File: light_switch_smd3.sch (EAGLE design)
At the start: 33 parts, among them U1 ESP8266_ESP-01

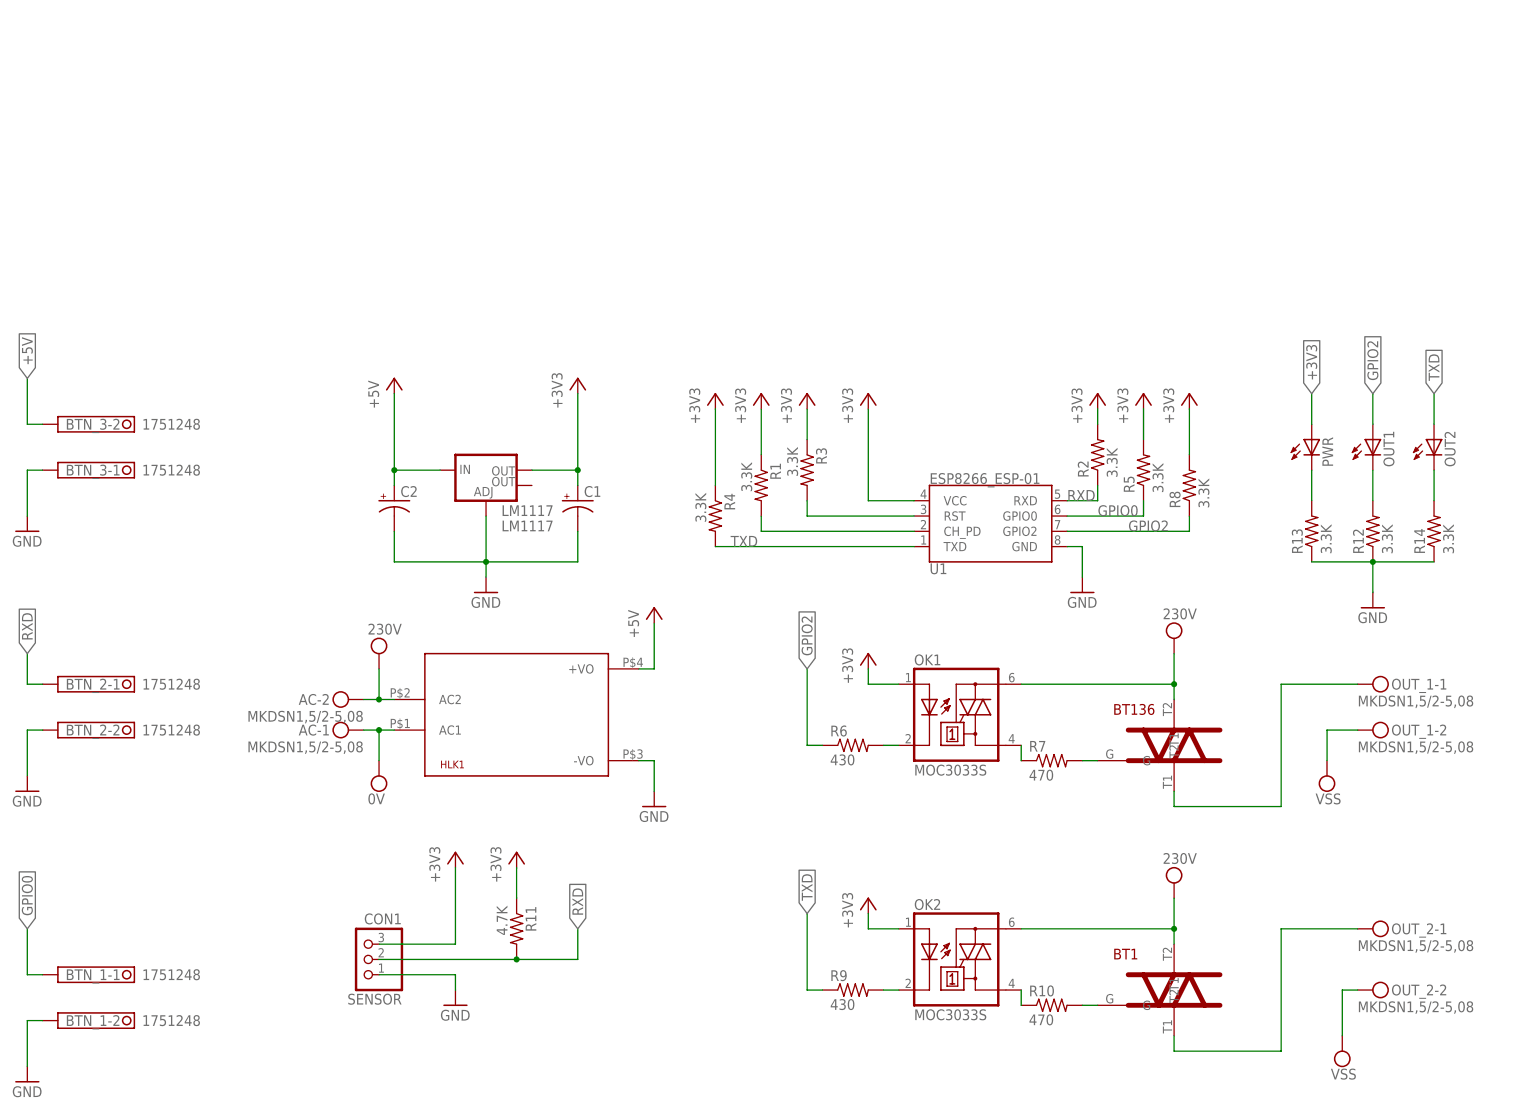
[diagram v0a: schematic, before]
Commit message: added pcf8574 due to undefined state of GPIOs during boot
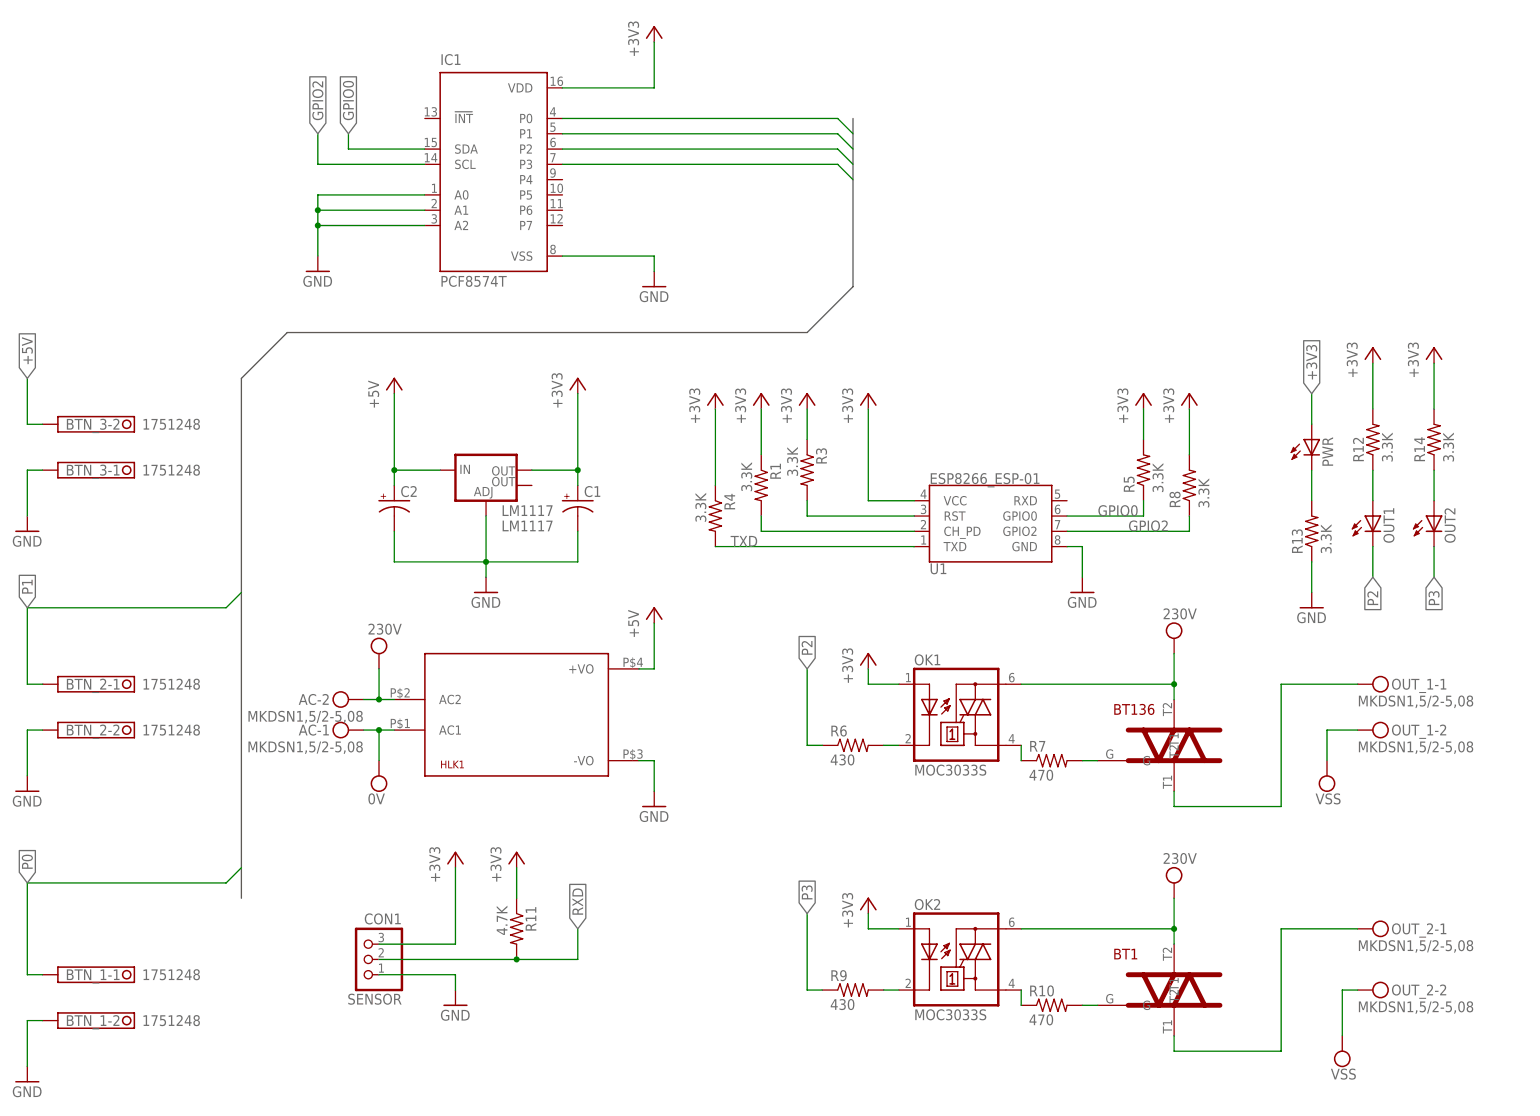
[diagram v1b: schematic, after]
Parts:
- removed R2: 3.3K, resistor:R-US_R1206
- added IC1: PCF8574T, micro-philips:PCF8574T
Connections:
- new net P0: BTN_1-1.K, IC1.P0
- new net P1: BTN_2-1.K, IC1.P1
- new net P2: IC1.P2, OUT1.C, R6.1
- new net P3: IC1.P3, OUT2.C, R9.1
- net +3V3: now also IC1.VDD, R12.2, R14.2; no longer R2.2
- net GND: now also IC1.A0, IC1.A1, IC1.A2, IC1.VSS; no longer R12.1, R14.1
- net GPIO0: now also IC1.SDA; no longer BTN_1-1.K
- net GPIO2: now also IC1.SCL; no longer OUT1.A, R6.1
- net N$11: now also OUT2.A, R14.1; no longer OUT2.C, R14.2
- net N$9: now also OUT1.A, R12.1; no longer OUT1.C, R12.2
- net RXD: no longer BTN_2-1.K, R2.1, U1.RXD
- net TXD: no longer OUT2.A, R9.1
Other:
- moved on the sheet: OUT1, OUT2, R12, R14

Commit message: DRC checked, no airwires
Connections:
- net RXD: now also U1.RXD
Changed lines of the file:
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@@
 <label x="101.6" y="35.56" size="1.778" layer="95" rot="R90" xref="yes"/>
+</segment>
+<segment>
+<pinref part="U1" gate="G$1" pin="RXD"/>
+<wire x1="182.88" y1="106.68" x2="185.42" y2="106.68" width="0.1524" layer="91"/>
+<wire x1="185.42" y1="106.68" x2="185.42" y2="116.84" width="0.1524" layer="91"/>
+<label x="185.42" y="116.84" size="1.778" layer="95" rot="R90" xref="yes"/>
 </segment>
 </net>

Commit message: added pinheader and small fixes
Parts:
- removed BTN_1, BTN_2: 1751248, con-phoenix-350:1751248
- added F1: (no value), fuse:TE5
- added JP1: (no value), pinhead:PINHD-1X4
- added X1: 1751251, con-phoenix-350:1751251
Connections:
- new net P4: IC1.P4, JP1.1
- new net P5: IC1.P5, JP1.2
- new net P6: IC1.P6, JP1.3
- new net P7: IC1.P7, JP1.4
- new net V230FUSE: BT1.T2, BT136.T2, F1.1, HLK1.AC2, OK1.A2, OK2.A2
- net GND: now also X1-2.K; no longer BTN_1-2.K, BTN_2-2.K
- net N$4: now also OUT_1-2.KL; no longer OUT_1-1.KL
- net N$8: now also OUT_2-2.KL; no longer OUT_2-1.KL
- net P0: now also X1-3.K; no longer BTN_1-1.K
- net P1: now also X1-1.K; no longer BTN_2-1.K
- net VPP: now also F1.2; no longer BT1.T2, BT136.T2, HLK1.AC2, OK1.A2, OK2.A2
- net VSS: now also OUT_1-1.KL, OUT_2-1.KL; no longer OUT_1-2.KL, OUT_2-2.KL
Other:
- moved on the sheet: OUT_1-1, OUT_1-2, OUT_2-1, OUT_2-2

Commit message: descriptions adjusted
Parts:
- renumbered BT1 to BT136., BTN_3 to POWER, F1 to FUSE, OUT_1 to OUT_P2, OUT_2 to OUT_P3
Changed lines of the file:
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@@
 <?xml version="1.0" encoding="utf-8"?>
 <!DOCTYPE eagle SYSTEM "eagle.dtd">
-<eagle version="9.3.0">
+<eagle version="9.5.2">
 <drawing>
 <settings>
@@
 <part name="U1" library="SparkFun-RF" deviceset="ESP8266_ESP-01" device=""/>
 <part name="AC" library="con-phoenix-508" deviceset="MKDSN1,5/2-5,08" device=""/>
-<part name="OUT_1" library="con-phoenix-508" deviceset="MKDSN1,5/2-5,08" device=""/>
-<part name="OUT_2" library="con-phoenix-508" deviceset="MKDSN1,5/2-5,08" device=""/>
+<part name="OUT_P2" library="con-phoenix-508" deviceset="MKDSN1,5/2-5,08" device=""/>
+<part name="OUT_P3" library="con-phoenix-508" deviceset="MKDSN1,5/2-5,08" device=""/>
 <part name="+3V1" library="supply1" deviceset="+3V3" device=""/>
 <part name="P+1" library="supply1" deviceset="+5V" device=""/>
@@
 <part name="R10" library="resistor" deviceset="R-US_" device="R1206" value="470"/>
 <part name="OK2" library="optocoupler" deviceset="MOC30*" device="S" technology="33"/>
-<part name="BT1" library="myblog_library" deviceset="BT136" device=""/>
+<part name="BT136." library="myblog_library" deviceset="BT136" device=""/>
 <part name="+3V10" library="supply1" deviceset="+3V3" device=""/>
 <part name="SUPPLY6" library="supply2" deviceset="VSS" device=""/>
@@
 <part name="R11" library="resistor" deviceset="R-US_" device="R1206" value="4.7K"/>
 <part name="+3V12" library="supply1" deviceset="+3V3" device=""/>
-<part name="BTN_3" library="con-phoenix-350" deviceset="1751248" device=""/>
+<part name="POWER" library="con-phoenix-350" deviceset="1751248" device=""/>
 <part name="GND7" library="supply1" deviceset="GND" device=""/>
 <part name="PWR" library="led" deviceset="LED" device="SML1206"/>
@@
 <part name="+3V2" library="supply1" deviceset="+3V3" device=""/>
 <part name="+3V14" library="supply1" deviceset="+3V3" device=""/>
-<part name="F1" library="fuse" library_urn="urn:adsk.eagle:library:233" deviceset="TE5" device="" package3d_urn="urn:adsk.eagle:package:14069/1"/>
+<part name="FUSE" library="fuse" library_urn="urn:adsk.eagle:library:233" deviceset="TE5" device="" package3d_urn="urn:adsk.eagle:package:14069/1"/>
 <part name="X1" library="con-phoenix-350" library_urn="urn:adsk.eagle:library:174" deviceset="1751251" device="" package3d_urn="urn:adsk.eagle:package:9394/1"/>
 <part name="JP1" library="pinhead" library_urn="urn:adsk.eagle:library:325" deviceset="PINHD-1X4" device="" package3d_urn="urn:adsk.eagle:package:22407/2"/>
@@
 <attribute name="VALUE" x="66.04" y="69.977" size="1.778" layer="96" rot="MR0"/>
 </instance>
-<instance part="OUT_1" gate="-1" x="233.68" y="68.58" smashed="yes">
+<instance part="OUT_P2" gate="-1" x="233.68" y="68.58" smashed="yes">
 <attribute name="NAME" x="236.728" y="67.691" size="1.778" layer="95"/>
 <attribute name="VALUE" x="231.14" y="64.897" size="1.778" layer="96"/>
 </instance>
-<instance part="OUT_1" gate="-2" x="233.68" y="76.2" smashed="yes">
+<instance part="OUT_P2" gate="-2" x="233.68" y="76.2" smashed="yes">
 <attribute name="NAME" x="236.728" y="75.311" size="1.778" layer="95"/>
 <attribute name="VALUE" x="231.14" y="72.517" size="1.778" layer="96"/>
 </instance>
-<instance part="OUT_2" gate="-1" x="236.22" y="25.4" smashed="yes">
+<instance part="OUT_P3" gate="-1" x="236.22" y="25.4" smashed="yes">
 <attribute name="NAME" x="239.268" y="24.511" size="1.778" layer="95"/>
 <attribute name="VALUE" x="233.68" y="21.717" size="1.778" layer="96"/>
 </instance>
-<instance part="OUT_2" gate="-2" x="236.22" y="35.56" smashed="yes">
+<instance part="OUT_P3" gate="-2" x="236.22" y="35.56" smashed="yes">
 <attribute name="NAME" x="239.268" y="34.671" size="1.778" layer="95"/>
 <attribute name="VALUE" x="233.68" y="31.877" size="1.778" layer="96"/>
@@
 <attribute name="VALUE" x="157.4546" y="20.3962" size="1.778" layer="96"/>
 </instance>
-<instance part="BT1" gate="G$1" x="200.66" y="25.4" smashed="yes">
+<instance part="BT136." gate="G$1" x="200.66" y="25.4" smashed="yes">
 <attribute name="NAME" x="190.5" y="30.48" size="1.778" layer="94"/>
 </instance>
@@
 <attribute name="VALUE" x="88.9" y="43.18" size="1.778" layer="96" rot="R90"/>
 </instance>
-<instance part="BTN_3" gate="-1" x="15.24" y="111.76" smashed="yes">
+<instance part="POWER" gate="-1" x="15.24" y="111.76" smashed="yes">
 <attribute name="NAME" x="16.51" y="110.871" size="1.778" layer="95"/>
 <attribute name="VALUE" x="29.21" y="110.871" size="1.778" layer="96"/>
 </instance>
-<instance part="BTN_3" gate="-2" x="15.24" y="119.38" smashed="yes">
+<instance part="POWER" gate="-2" x="15.24" y="119.38" smashed="yes">
 <attribute name="NAME" x="16.51" y="118.491" size="1.778" layer="95"/>
 <attribute name="VALUE" x="29.21" y="118.491" size="1.778" layer="96"/>
@@
 <attribute name="VALUE" x="241.3" y="127" size="1.778" layer="96" rot="R90"/>
 </instance>
-<instance part="F1" gate="1" x="195.58" y="142.24" smashed="yes">
+<instance part="FUSE" gate="1" x="195.58" y="142.24" smashed="yes">
 <attribute name="NAME" x="191.77" y="143.637" size="1.778" layer="95"/>
 <attribute name="VALUE" x="191.77" y="139.319" size="1.778" layer="96"/>
@@
 <pinref part="GND7" gate="1" pin="GND"/>
 <wire x1="10.16" y1="104.14" x2="10.16" y2="111.76" width="0.1524" layer="91"/>
-<pinref part="BTN_3" gate="-1" pin="K"/>
+<pinref part="POWER" gate="-1" pin="K"/>
 <wire x1="12.7" y1="111.76" x2="10.16" y2="111.76" width="0.1524" layer="91"/>
 </segment>
@@
 <wire x1="10.16" y1="119.38" x2="10.16" y2="127" width="0.1524" layer="91"/>
 <label x="10.16" y="127" size="1.778" layer="95" rot="R90" xref="yes"/>
-<pinref part="BTN_3" gate="-2" pin="K"/>
+<pinref part="POWER" gate="-2" pin="K"/>
 <wire x1="12.7" y1="119.38" x2="10.16" y2="119.38" width="0.1524" layer="91"/>
 </segment>
@@
 </segment>
 <segment>
-<pinref part="F1" gate="1" pin="2"/>
+<pinref part="FUSE" gate="1" pin="2"/>
 <pinref part="SUPPLY4" gate="G$1" pin="VPP"/>
 <wire x1="200.66" y1="142.24" x2="208.28" y2="142.24" width="0.1524" layer="91"/>
@@
 <pinref part="SUPPLY3" gate="G$1" pin="VSS"/>
 <wire x1="226.06" y1="68.58" x2="226.06" y2="63.5" width="0.1524" layer="91"/>
-<pinref part="OUT_1" gate="-1" pin="KL"/>
+<pinref part="OUT_P2" gate="-1" pin="KL"/>
 <wire x1="231.14" y1="68.58" x2="226.06" y2="68.58" width="0.1524" layer="91"/>
 </segment>
@@
 <pinref part="SUPPLY6" gate="G$1" pin="VSS"/>
 <wire x1="228.6" y1="25.4" x2="228.6" y2="17.78" width="0.1524" layer="91"/>
-<pinref part="OUT_2" gate="-1" pin="KL"/>
+<pinref part="OUT_P3" gate="-1" pin="KL"/>
 <wire x1="233.68" y1="25.4" x2="228.6" y2="25.4" width="0.1524" layer="91"/>
 </segment>
@@
 <segment>
 <pinref part="R10" gate="G$1" pin="2"/>
-<pinref part="BT1" gate="G$1" pin="G"/>
+<pinref part="BT136." gate="G$1" pin="G"/>
 <wire x1="185.42" y1="22.86" x2="187.96" y2="22.86" width="0.1524" layer="91"/>
 </segment>
@@
 <wire x1="200.66" y1="55.88" x2="218.44" y2="55.88" width="0.1524" layer="91"/>
 <wire x1="218.44" y1="55.88" x2="218.44" y2="76.2" width="0.1524" layer="91"/>
-<pinref part="OUT_1" gate="-2" pin="KL"/>
+<pinref part="OUT_P2" gate="-2" pin="KL"/>
 <wire x1="231.14" y1="76.2" x2="218.44" y2="76.2" width="0.1524" layer="91"/>
 </segment>
@@
 <net name="N$8" class="0">
 <segment>
-<pinref part="BT1" gate="G$1" pin="T1"/>
+<pinref part="BT136." gate="G$1" pin="T1"/>
 <wire x1="200.66" y1="17.78" x2="200.66" y2="15.24" width="0.1524" layer="91"/>
 <wire x1="200.66" y1="15.24" x2="218.44" y2="15.24" width="0.1524" layer="91"/>
 <wire x1="218.44" y1="15.24" x2="218.44" y2="35.56" width="0.1524" layer="91"/>
-<pinref part="OUT_2" gate="-2" pin="KL"/>
+<pinref part="OUT_P3" gate="-2" pin="KL"/>
 <wire x1="233.68" y1="35.56" x2="218.44" y2="35.56" width="0.1524" layer="91"/>
 </segment>
@@
 <net name="V230FUSE" class="0">
 <segment>
-<pinref part="F1" gate="1" pin="1"/>
+<pinref part="FUSE" gate="1" pin="1"/>
 <wire x1="190.5" y1="142.24" x2="182.88" y2="142.24" width="0.1524" layer="91"/>
 <label x="182.88" y="142.24" size="1.778" layer="95" rot="R90" xref="yes"/>
@@
 <pinref part="OK2" gate="-1" pin="A2"/>
 <wire x1="175.26" y1="35.56" x2="200.66" y2="35.56" width="0.1524" layer="91"/>
-<pinref part="BT1" gate="G$1" pin="T2"/>
+<pinref part="BT136." gate="G$1" pin="T2"/>
 <wire x1="200.66" y1="33.02" x2="200.66" y2="35.56" width="0.1524" layer="91"/>
 <wire x1="200.66" y1="40.64" x2="200.66" y2="35.56" width="0.1524" layer="91"/>
